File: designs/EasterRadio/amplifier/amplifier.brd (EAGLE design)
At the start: 31 x 34 mm, 14 parts, among them IC1 PAM8403DR, J1 STX-3120-3BM, J2 S2B-NSHSS-TB, J3 S2B-NSHSS-TB

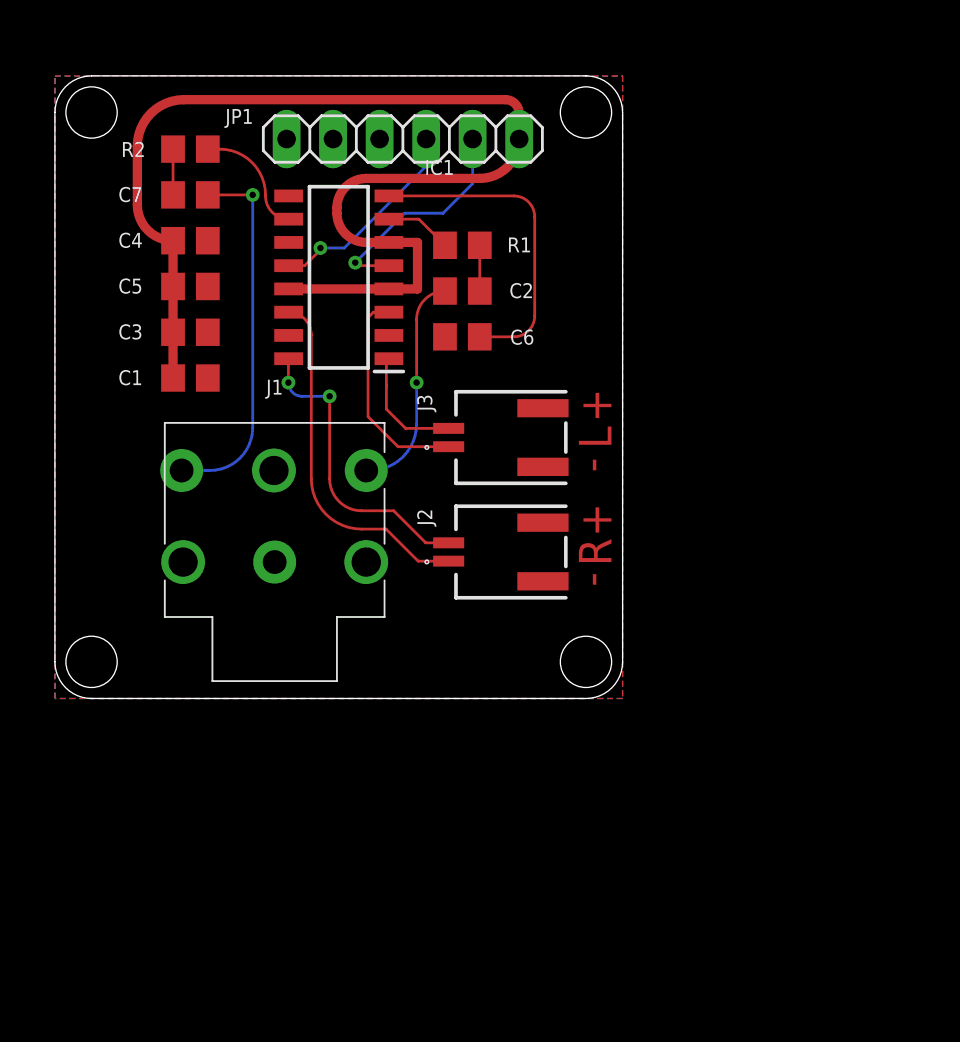
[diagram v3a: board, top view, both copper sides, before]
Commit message: added final power and amplifier design and ESP32 E footprint
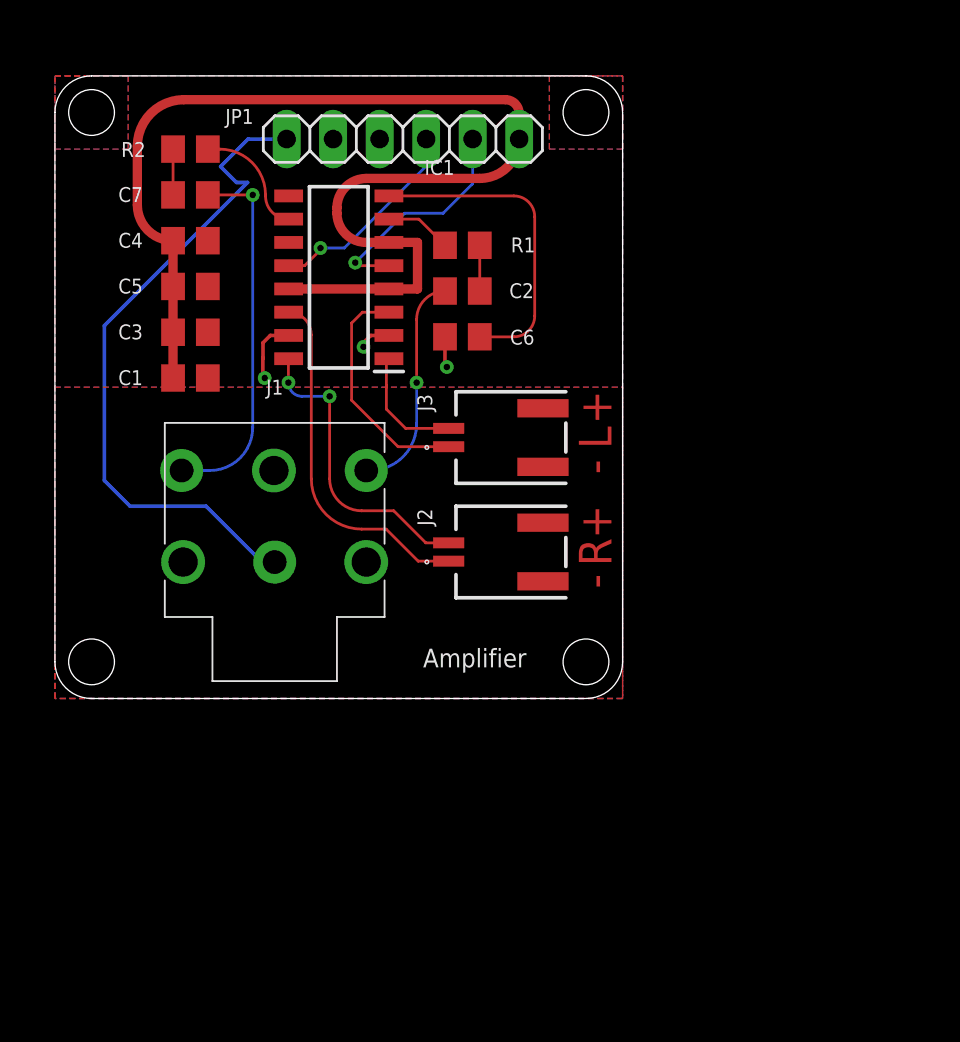
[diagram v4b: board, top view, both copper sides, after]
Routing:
- net AGND: track 0.00 -> 43.7 mm, vias 0 -> 3
- net OUT_L-: track 11.8 -> 12.8 mm
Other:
- board text added: "Amplifier"
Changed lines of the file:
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@@
 <setting verticaltext="up"/>
 </settings>
-<grid distance="0.1" unitdist="mm" unit="mm" style="lines" multiple="1" display="yes" altdistance="5" altunitdist="mil" altunit="mil"/>
+<grid distance="1" unitdist="mm" unit="mm" style="lines" multiple="1" display="yes" altdistance="5" altunitdist="mil" altunit="mil"/>
 <layers>
 <layer number="1" name="Top" color="4" fill="1" visible="yes" active="yes"/>
@@
 <layer number="27" name="tValues" color="7" fill="1" visible="yes" active="yes"/>
 <layer number="28" name="bValues" color="7" fill="1" visible="yes" active="yes"/>
-<layer number="29" name="tStop" color="7" fill="3" visible="no" active="yes"/>
+<layer number="29" name="tStop" color="7" fill="3" visible="yes" active="yes"/>
 <layer number="30" name="bStop" color="7" fill="6" visible="no" active="yes"/>
 <layer number="31" name="tCream" color="7" fill="4" visible="no" active="yes"/>
@@
 <wire x1="31" y1="2" x2="31" y2="32" width="0" layer="20"/>
 <wire x1="31" y1="32" x2="29" y2="34" width="0" layer="20" curve="90"/>
-<hole x="29" y="32" drill="2.8"/>
-<hole x="2" y="2" drill="2.8"/>
-<hole x="29" y="2" drill="2.8"/>
-<hole x="2" y="32" drill="2.8"/>
+<hole x="29" y="32" drill="2.5"/>
+<hole x="2" y="2" drill="2.5"/>
+<hole x="29" y="2" drill="2.5"/>
+<hole x="2" y="32" drill="2.5"/>
 <text x="29.5" y="8" size="1.778" layer="1" font="vector" ratio="15" rot="R90" align="center">R</text>
 <text x="29.5" y="14.25" size="1.778" layer="1" font="vector" ratio="15" rot="R90" align="center">L</text>
-<text x="29.5" y="16" size="1.778" layer="1" font="vector" ratio="15" rot="R90" align="center">+</text>
-<text x="29.25" y="12.75" size="1.778" layer="1" font="vector" ratio="15" rot="R90" align="center">-</text>
-<text x="29.5" y="9.75" size="1.778" layer="1" font="vector" ratio="15" rot="R90" align="center">+</text>
-<text x="29.25" y="6.5" size="1.778" layer="1" font="vector" ratio="15" rot="R90" align="center">-</text>
+<text x="29.5" y="15.9" size="1.778" layer="1" font="vector" ratio="15" rot="R90" align="center">+</text>
+<text x="29.45" y="12.65" size="1.778" layer="1" font="vector" ratio="15" rot="R90" align="center">-</text>
+<text x="29.5" y="9.65" size="1.778" layer="1" font="vector" ratio="15" rot="R90" align="center">+</text>
+<text x="29.45" y="6.4" size="1.778" layer="1" font="vector" ratio="15" rot="R90" align="center">-</text>
 <text x="29.5" y="8" size="1.778" layer="29" font="vector" ratio="15" rot="R90" align="center">R</text>
-<text x="29.5" y="9.75" size="1.778" layer="29" font="vector" ratio="15" rot="R90" align="center">+</text>
-<text x="29.25" y="6.5" size="1.778" layer="29" font="vector" ratio="15" rot="R90" align="center">-</text>
+<text x="29.5" y="9.65" size="1.778" layer="29" font="vector" ratio="15" rot="R90" align="center">+</text>
+<text x="29.45" y="6.4" size="1.778" layer="29" font="vector" ratio="15" rot="R90" align="center">-</text>
 <text x="29.5" y="14.25" size="1.778" layer="29" font="vector" ratio="15" rot="R90" align="center">L</text>
-<text x="29.5" y="16" size="1.778" layer="29" font="vector" ratio="15" rot="R90" align="center">+</text>
-<text x="29.25" y="12.75" size="1.778" layer="29" font="vector" ratio="15" rot="R90" align="center">-</text>
+<text x="29.5" y="15.9" size="1.778" layer="29" font="vector" ratio="15" rot="R90" align="center">+</text>
+<text x="29.45" y="12.65" size="1.778" layer="29" font="vector" ratio="15" rot="R90" align="center">-</text>
+<text x="20.1" y="1.7" size="1.016" layer="25">Amplifier</text>
 </plain>
 <attributes>
@@
 <param name="srMinRoundness" value="0.1mm"/>
 <param name="srMaxRoundness" value="0.1mm"/>
-<param name="slThermalIsolate" value="0.1mm"/>
-<param name="slThermalsForVias" value="0"/>
-<param name="dpMaxLengthDifference" value="10mm"/>
+<param name="slThermalIsolate" value="0.2mm"/>
+<param name="slThermalsForVias" value="1"/>
+<param name="dpMaxLengthDifference" value="0.1mm"/>
 <param name="dpGapFactor" value="2.5"/>
 <param name="checkAngle" value="0"/>
@@
 </element>
 <element name="R1" library="CommonParts" package="R0805" package3d_urn="urn:adsk.eagle:package:23553/2" value="10k" x="22.25" y="24.75" smashed="yes">
-<attribute name="NAME" x="25.365" y="24.77" size="0.8128" layer="25" align="center"/>
+<attribute name="NAME" x="25.565" y="24.77" size="0.8128" layer="25" align="center"/>
 </element>
 <element name="C2" library="CommonParts" package="C0805" package3d_urn="urn:adsk.eagle:package:23617/2" value="0.47uF" x="22.25" y="22.25" smashed="yes">
@@
 <contactref element="J1" pad="1"/>
 <contactref element="JP1" pad="1"/>
-<polygon width="0" layer="1">
+<polygon width="0.2" layer="1">
 <vertex x="0" y="34"/>
 <vertex x="31" y="34"/>
@@
 <vertex x="0" y="0"/>
 </polygon>
-<polygon width="0" layer="16">
+<polygon width="0.2" layer="16">
 <vertex x="0" y="34"/>
 <vertex x="31" y="34"/>
 <vertex x="31" y="0"/>
 <vertex x="0" y="0"/>
+</polygon>
+<polygon width="0" layer="1" pour="cutout" isolate="0.3048">
+<vertex x="0" y="17"/>
+<vertex x="31" y="17"/>
+<vertex x="31" y="0"/>
+<vertex x="0" y="0"/>
+</polygon>
+<polygon width="0" layer="16" pour="cutout" isolate="0.3048">
+<vertex x="0" y="17"/>
+<vertex x="31" y="17"/>
+<vertex x="31" y="0"/>
+<vertex x="0" y="0"/>
+</polygon>
+<wire x1="12" y1="7.45" x2="11.3" y2="7.45" width="0.2" layer="16"/>
+<wire x1="2.7" y1="20.359125" x2="10.519075" y2="28.1782" width="0.2" layer="16"/>
+<wire x1="10.519075" y1="28.1782" x2="9.915075" y2="28.1782" width="0.2" layer="16"/>
+<wire x1="9.915075" y1="28.1782" x2="9.0466375" y2="29.0466375" width="0.2" layer="16"/>
+<wire x1="9.0466375" y1="29.0466375" x2="10.55" y2="30.55" width="0.2" layer="16"/>
+<wire x1="10.55" y1="30.55" x2="12.65" y2="30.55" width="0.2" layer="16"/>
+<wire x1="8.25" y1="10.5" x2="4.1" y2="10.5" width="0.2" layer="16"/>
+<wire x1="4.1" y1="10.5" x2="2.7" y2="11.9" width="0.2" layer="16"/>
+<wire x1="11.3" y1="7.45" x2="8.25" y2="10.5" width="0.2" layer="16"/>
+<wire x1="2.7" y1="11.9" x2="2.7" y2="20.359125" width="0.2" layer="16"/>
+<wire x1="11.4544" y1="17.5" x2="11.3544" y2="17.6" width="0.2" layer="1"/>
+<wire x1="11.3544" y1="18.5848" x2="11.3544" y2="17.6" width="0.2" layer="1"/>
+<wire x1="11.362" y1="18.5924" x2="11.3544" y2="18.5848" width="0.2" layer="1"/>
+<wire x1="12.762" y1="19.825" x2="11.762" y2="19.825" width="0.2" layer="1"/>
+<wire x1="11.762" y1="19.825" x2="11.362" y2="19.425" width="0.2" layer="1"/>
+<wire x1="11.362" y1="19.425" x2="11.362" y2="18.5924" width="0.2" layer="1"/>
+<via x="11.4544" y="17.5" extent="1-16" drill="0.35"/>
+<via x="16.8544" y="19.2" extent="1-16" drill="0.35"/>
+<wire x1="18.238" y1="19.825" x2="17.2462375" y2="19.825" width="0.2" layer="1"/>
+<wire x1="17.2462375" y1="19.825" x2="16.8544" y2="19.4331625" width="0.2" layer="1"/>
+<wire x1="16.8544" y1="19.2" x2="16.8544" y2="19.4331625" width="0.2" layer="1"/>
+<wire x1="21.3" y1="19.75" x2="21.3" y2="18.2" width="0.2" layer="1"/>
+<wire x1="21.3" y1="18.2" x2="21.4" y2="18.1" width="0.2" layer="1"/>
+<via x="21.4" y="18.1" extent="1-16" drill="0.35"/>
+<polygon width="0" layer="16" pour="cutout" isolate="0.3048">
+<vertex x="0" y="34"/>
+<vertex x="4" y="34"/>
+<vertex x="4" y="30"/>
+<vertex x="0" y="30"/>
+</polygon>
+<polygon width="0" layer="16" pour="cutout" isolate="0.3048">
+<vertex x="27" y="34"/>
+<vertex x="27" y="30"/>
+<vertex x="31" y="30"/>
+<vertex x="31" y="34"/>
+</polygon>
+<polygon width="0" layer="1" pour="cutout" isolate="0.3048">
+<vertex x="0" y="30"/>
+<vertex x="4" y="30"/>
+<vertex x="4" y="34"/>
+<vertex x="0" y="34"/>
+</polygon>
+<polygon width="0" layer="1" pour="cutout" isolate="0.3048">
+<vertex x="27" y="34"/>
+<vertex x="27" y="30"/>
+<vertex x="31" y="30"/>
+<vertex x="31" y="34"/>
 </polygon>
 </signal>
@@
 <wire x1="17" y1="28.4" x2="23.2" y2="28.4" width="0.508" layer="1"/>
 <wire x1="23.2" y1="28.4" x2="25.35" y2="30.55" width="0.508" layer="1" curve="90"/>
-<wire x1="25.4" y1="30.6" x2="25.35" y2="30.55" width="0.508" layer="1"/>
 <wire x1="25.35" y1="30.55" x2="25.35" y2="31.95" width="0.508" layer="1"/>
 <wire x1="25.35" y1="31.95" x2="24.6" y2="32.7" width="0.508" layer="1" curve="90"/>
@@
 <contactref element="J3" pad="1"/>
 <wire x1="21.5" y1="13.75" x2="18.735775" y2="13.75" width="0.1524" layer="1"/>
-<wire x1="18.735775" y1="13.75" x2="17.1" y2="15.385775" width="0.1524" layer="1"/>
-<wire x1="17.395" y1="21.095" x2="18.238" y2="21.095" width="0.1524" layer="1"/>
-<wire x1="17.1" y1="15.385775" x2="17.1" y2="20.8" width="0.1524" layer="1"/>
-<wire x1="17.1" y1="20.8" x2="17.395" y2="21.095" width="0.1524" layer="1"/>
+<wire x1="18.735775" y1="13.75" x2="16.2" y2="16.285775" width="0.1524" layer="1"/>
+<wire x1="16.795" y1="21.095" x2="18.238" y2="21.095" width="0.1524" layer="1"/>
+<wire x1="16.2" y1="16.285775" x2="16.2" y2="20.5" width="0.1524" layer="1"/>
+<wire x1="16.2" y1="20.5" x2="16.795" y2="21.095" width="0.1524" layer="1"/>
 </signal>
 <signal name="!MUTE">
@@
 </signals>
 <mfgpreviewcolors>
-<mfgpreviewcolor name="soldermaskcolor" color="0xC8008000"/>
+<mfgpreviewcolor name="soldermaskcolor" color="0xC8000000"/>
 <mfgpreviewcolor name="silkscreencolor" color="0xFFFEFEFE"/>
 <mfgpreviewcolor name="backgroundcolor" color="0xFF282828"/>

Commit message: everything pushed to fusion
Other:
- board size 31 x 34 mm -> 33 x 36 mm
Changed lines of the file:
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@@
 </layers>
 <board>
+<fusionsync huburn="a.cGVyc29uYWw6dWUyYTNmMDU1" projecturn="a.cGVyc29uYWw6dWUyYTNmMDU1IzIwMTgxMjEwMTY0OTQ5MjI2" f3durn="urn:adsk.wipprod:dm.lineage:GdUElHh-Ssm79hANlXEZ3w" pcbguid="4bd99cf8-ae48-4c13-9cbd-003edd884035" lastpulledtime="" lastsyncedchangeguid="" latestrevisionid="5f272d40-25d0-4105-a02c-6fd692911643" lastsyncedrevisionid="5f272d40-25d0-4105-a02c-6fd692911643" lastboardhashguid="d37c62de-a670-4ebf-3550-101a40fdde36" lastpushedtime="2020-11-28T17:19:50Z" linktopcb3d="true"/>
 <plain>
-<wire x1="29" y1="34" x2="2" y2="34" width="0" layer="20"/>
-<wire x1="2" y1="34" x2="0" y2="32" width="0" layer="20" curve="90"/>
-<wire x1="0" y1="32" x2="0" y2="2" width="0" layer="20"/>
-<wire x1="0" y1="2" x2="2" y2="0" width="0" layer="20" curve="90"/>
-<wire x1="2" y1="0" x2="29" y2="0" width="0" layer="20"/>
-<wire x1="29" y1="0" x2="31" y2="2" width="0" layer="20" curve="90"/>
-<wire x1="31" y1="2" x2="31" y2="32" width="0" layer="20"/>
-<wire x1="31" y1="32" x2="29" y2="34" width="0" layer="20" curve="90"/>
+<wire x1="32" y1="1" x2="32" y2="33" width="0" layer="20"/>
+<wire x1="32" y1="33" x2="30" y2="35" width="0" layer="20"/>
+<wire x1="30" y1="35" x2="1" y2="35" width="0" layer="20"/>
+<wire x1="1" y1="35" x2="-1" y2="33" width="0" layer="20"/>
+<wire x1="-1" y1="33" x2="-1" y2="1" width="0" layer="20"/>
+<wire x1="-1" y1="1" x2="1" y2="-1" width="0" layer="20"/>
+<wire x1="1" y1="-1" x2="30" y2="-1" width="0" layer="20"/>
+<wire x1="30" y1="-1" x2="32" y2="1" width="0" layer="20"/>
 <hole x="29" y="32" drill="2.5"/>
 <hole x="2" y="2" drill="2.5"/>
@@
 <text x="29.5" y="15.9" size="1.778" layer="29" font="vector" ratio="15" rot="R90" align="center">+</text>
 <text x="29.45" y="12.65" size="1.778" layer="29" font="vector" ratio="15" rot="R90" align="center">-</text>
-<text x="20.1" y="1.7" size="1.016" layer="25">Amplifier</text>
+<circle x="2" y="32" radius="1" width="2.54" layer="41"/>
+<circle x="2" y="2" radius="1" width="2.54" layer="41"/>
+<circle x="29" y="2" radius="1" width="2.54" layer="41"/>
+<circle x="29" y="32" radius="1" width="2.54" layer="41"/>
+<text x="29.3" y="18.1" size="1.778" layer="1" font="vector" ratio="15" rot="R90">Amplifier</text>
+<text x="29.3" y="18.1" size="1.778" layer="29" font="vector" ratio="15" rot="R90">Amplifier</text>
 </plain>
 <attributes>
@@
 <contactref element="JP1" pad="1"/>
 <polygon width="0.2" layer="1">
-<vertex x="0" y="34"/>
-<vertex x="31" y="34"/>
-<vertex x="31" y="0"/>
-<vertex x="0" y="0"/>
+<vertex x="-1" y="35"/>
+<vertex x="32" y="35"/>
+<vertex x="32" y="-1"/>
+<vertex x="-1" y="-1"/>
 </polygon>
 <polygon width="0.2" layer="16">
-<vertex x="0" y="34"/>
-<vertex x="31" y="34"/>
-<vertex x="31" y="0"/>
-<vertex x="0" y="0"/>
+<vertex x="-1" y="35"/>
+<vertex x="32" y="35"/>
+<vertex x="32" y="-1"/>
+<vertex x="-1" y="-1"/>
 </polygon>
 <polygon width="0" layer="1" pour="cutout" isolate="0.3048">
 <vertex x="0" y="17"/>
-<vertex x="31" y="17"/>
-<vertex x="31" y="0"/>
-<vertex x="0" y="0"/>
+<vertex x="32" y="17"/>
+<vertex x="32" y="-1"/>
+<vertex x="0" y="-1"/>
 </polygon>
 <polygon width="0" layer="16" pour="cutout" isolate="0.3048">
-<vertex x="0" y="17"/>
-<vertex x="31" y="17"/>
-<vertex x="31" y="0"/>
-<vertex x="0" y="0"/>
+<vertex x="-1" y="17"/>
+<vertex x="32" y="17"/>
+<vertex x="32" y="-1"/>
+<vertex x="-1" y="-1"/>
 </polygon>
 <wire x1="12" y1="7.45" x2="11.3" y2="7.45" width="0.2" layer="16"/>
@@
 <wire x1="21.3" y1="18.2" x2="21.4" y2="18.1" width="0.2" layer="1"/>
 <via x="21.4" y="18.1" extent="1-16" drill="0.35"/>
-<polygon width="0" layer="16" pour="cutout" isolate="0.3048">
-<vertex x="0" y="34"/>
-<vertex x="4" y="34"/>
-<vertex x="4" y="30"/>
-<vertex x="0" y="30"/>
-</polygon>
-<polygon width="0" layer="16" pour="cutout" isolate="0.3048">
-<vertex x="27" y="34"/>
-<vertex x="27" y="30"/>
-<vertex x="31" y="30"/>
-<vertex x="31" y="34"/>
-</polygon>
-<polygon width="0" layer="1" pour="cutout" isolate="0.3048">
-<vertex x="0" y="30"/>
-<vertex x="4" y="30"/>
-<vertex x="4" y="34"/>
-<vertex x="0" y="34"/>
-</polygon>
-<polygon width="0" layer="1" pour="cutout" isolate="0.3048">
-<vertex x="27" y="34"/>
-<vertex x="27" y="30"/>
-<vertex x="31" y="30"/>
-<vertex x="31" y="34"/>
-</polygon>
 </signal>
 <signal name="INR">
@@
 </note>
 <note version="8.3" severity="warning">
+Since Version 8.3, EAGLE supports Fusion synchronisation.
+This feature will not be available in this version and saving
+the document will break the link to the Fusion PCB feature.
+</note>
+<note version="8.3" severity="warning">
